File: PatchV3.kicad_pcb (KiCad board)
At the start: 4 copper layers, 100 x 50 mm, 104 parts, among them J1 Conn_01x05, J2 2908-05WB-MG, J3 JST PH SM4 S2B, J4 JST PH SM4 S2B, U1 STM32WB5MMGH6TR_1-, U2 INA317IDGKT, U3 INA317IDGKT, U4 OPA2349EA_250, U5 OPA2349EA_250, U6 ADP5091ACPZ-1-R7, U7 LT3009IDCTRMPBF, U8 LT3009IDCTRMPBF

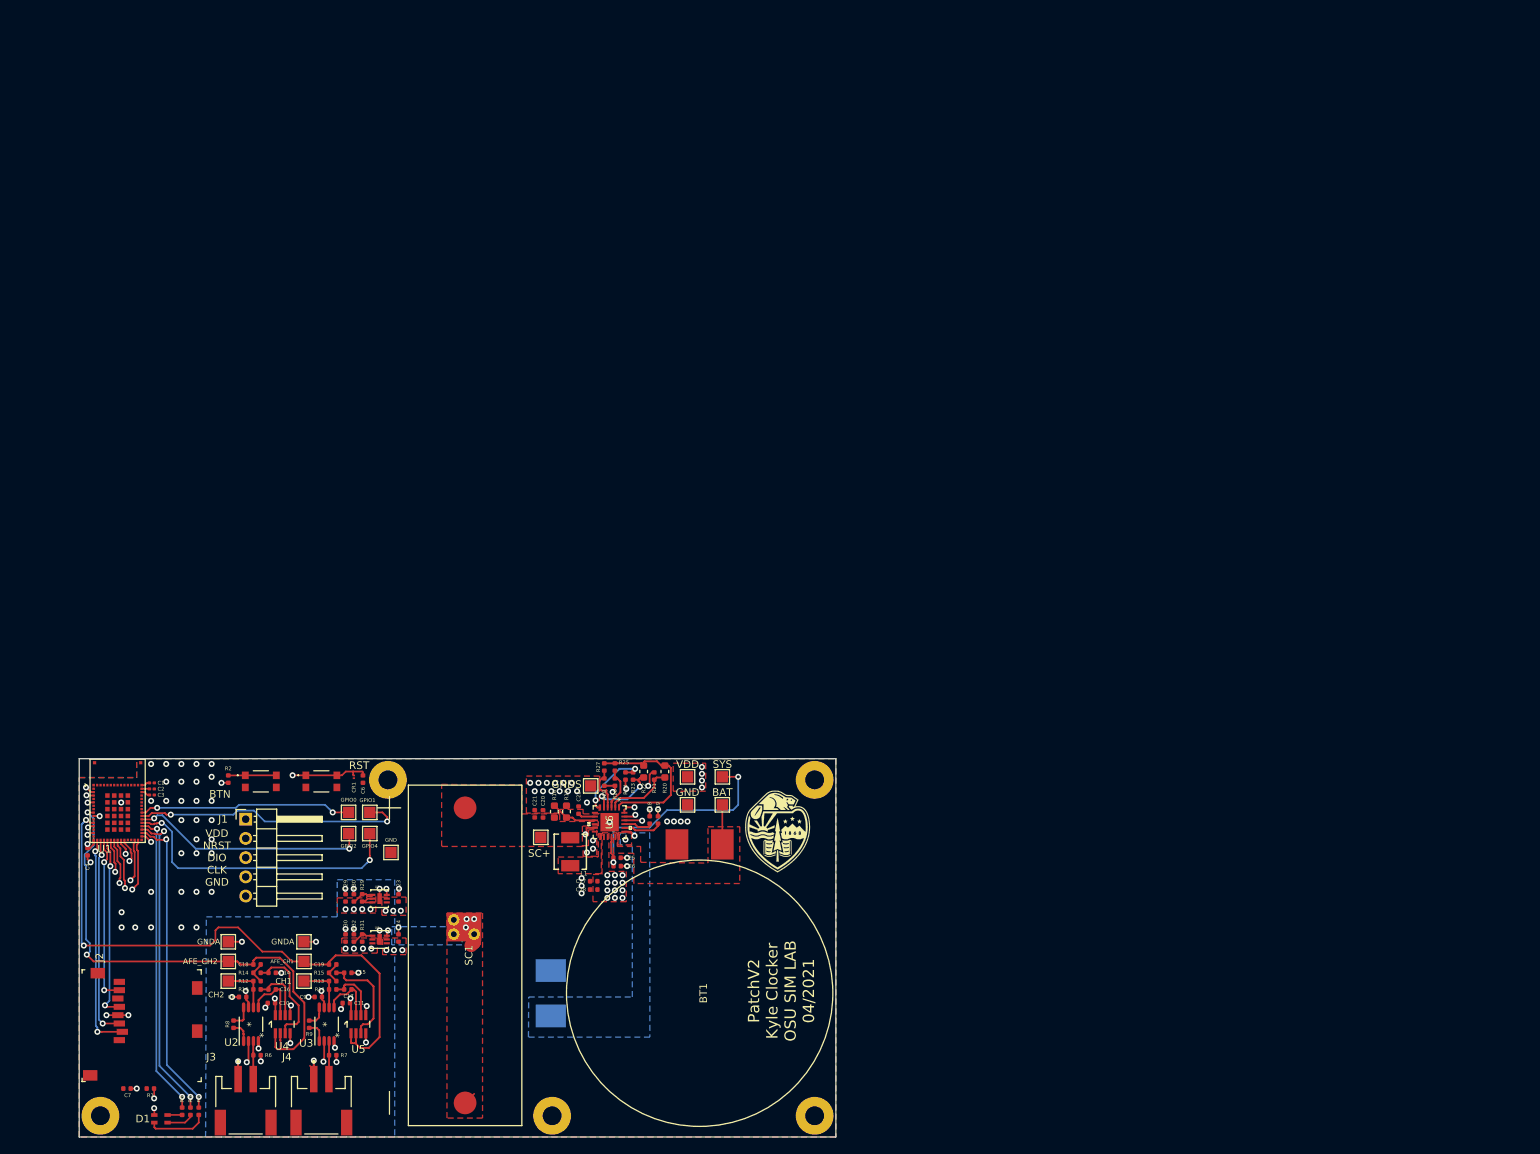
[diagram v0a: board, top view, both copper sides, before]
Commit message: schematic functionally finished working on layout
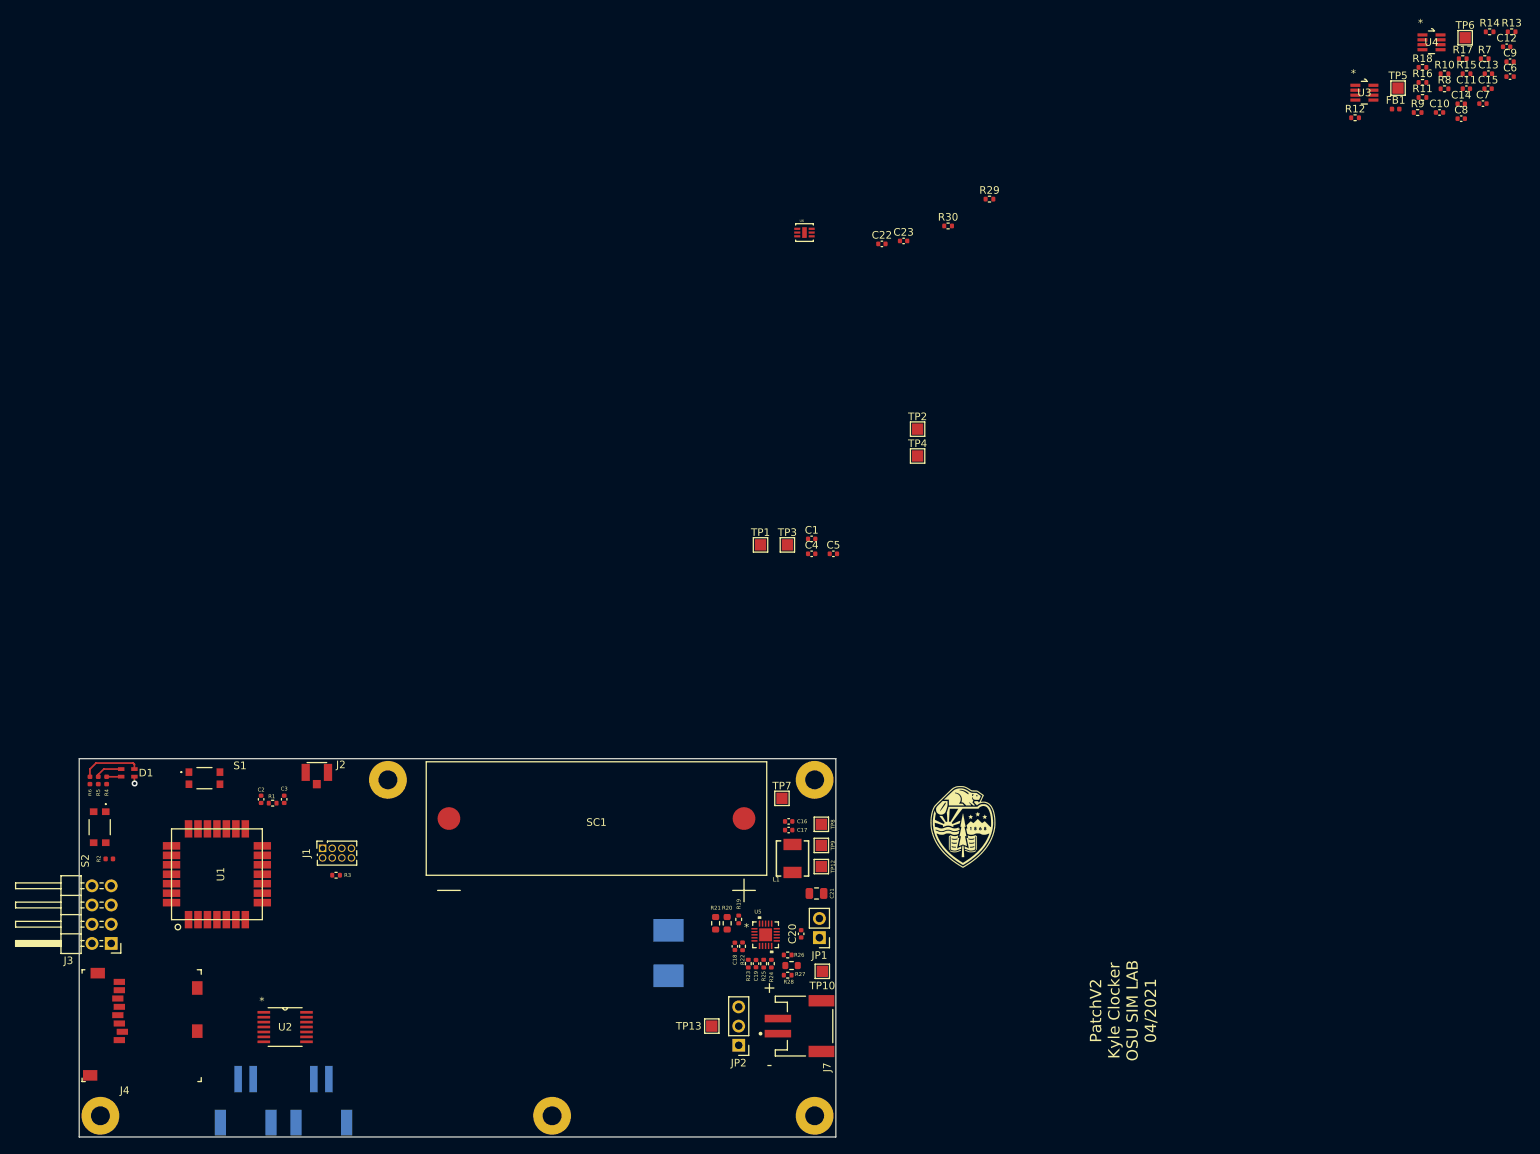
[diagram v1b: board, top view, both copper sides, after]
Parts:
- removed AFE_CH1, AFE_CH2, BAT, CH1, CH2, GND (x2), GNDA (x2), GNDS, GPIO0, GPIO1, GPIO2, GPIO4, SC+, SYS, VDD: TestPoint, TestPoint:TestPoint_Pad_1.5x1.5mm
- removed BT2: 3.7V 500mAh, PatchV2:RJD-ST1
- removed BTN, RST: KMR742NGLFS, PatchV2:KMR742NGLFS
- removed C24, C25, C27, C29, C30: 0.1uF, Capacitor_SMD:C_0402_1005Metric
- removed C26, C28: 10uF, Capacitor_SMD:C_0402_1005Metric
- removed CR1: ESDALC6V1-1U2, PatchV2:ESDALC6V1-1U2
- removed NT1: Net-Tie_3_Tee, PatchV2:gnd_tie
- removed R31: 301k 1%, Resistor_SMD:R_0402_1005Metric
- removed R32: 604k 0.1%, Resistor_SMD:R_0402_1005Metric
- removed the R6 at (73.5, 89.2)
- removed U7, U8: LT3009IDCTRMPBF, PatchV2:DFN-6_DC
- added C12: 0.1uF, Capacitor_SMD:C_0402_1005Metric, F.Cu at (238.7, -44.1)
- added C13: 0.1uF, Capacitor_SMD:C_0402_1005Metric, F.Cu at (236.2, -40.5)
- added C5: 0.1uF, Capacitor_SMD:C_0402_1005Metric, F.Cu at (149.7, 22.9)
- added FB1: 600 Ohm, Inductor_SMD:L_0402_1005Metric, F.Cu at (224.0, -35.9)
- added J2: U.FL-R-SMT(01), PatchV2:HRS_U.FL-R-SMT(01), F.Cu at (81.4, 51.8)
- added J3: Conn_02x04_Odd_Even, Connector_PinHeader_2.54mm:PinHeader_2x04_P2.54mm_Horizontal, F.Cu at (54.2, 74.4)
- added J7: JST PH SM4 S2B, PatchV2:JST-S2B-PH-SM4-TBLFSN-Manufacturer_Recommended, F.Cu at (145.8, 85.3)
- added JP1: Jumper, Connector_PinHeader_2.54mm:PinHeader_1x02_P2.54mm_Vertical, F.Cu at (147.8, 73.7)
- added JP2: Jumper_NC_Dual, Connector_PinHeader_2.54mm:PinHeader_1x03_P2.54mm_Vertical, F.Cu at (137.2, 87.9)
- added R3: 0, Resistor_SMD:R_0402_1005Metric, F.Cu at (83.9, 65.4)
- added S1: KMR742NGLFS, PatchV2:KMR742NGLFS, F.Cu at (66.5, 52.6)
- added S2: KMR742NGLFS, PatchV2:KMR742NGLFS, F.Cu at (52.7, 59.1)
- added TP1: TestPoint, TestPoint:TestPoint_Pad_1.5x1.5mm, F.Cu at (140.0, 21.7)
- added TP10: TestPoint, TestPoint:TestPoint_Pad_1.5x1.5mm, F.Cu at (148.2, 78.1)
- added TP12: TestPoint, TestPoint:TestPoint_Pad_1.5x1.5mm, F.Cu at (148.1, 64.3)
- added TP13: TestPoint, TestPoint:TestPoint_Pad_1.5x1.5mm, F.Cu at (133.6, 85.3)
- added TP2: TestPoint, TestPoint:TestPoint_Pad_1.5x1.5mm, F.Cu at (160.8, 6.45)
- added TP3: TestPoint, TestPoint:TestPoint_Pad_1.5x1.5mm, F.Cu at (143.6, 21.7)
- added TP4: TestPoint, TestPoint:TestPoint_Pad_1.5x1.5mm, F.Cu at (160.8, 9.99)
- added TP5: TestPoint, TestPoint:TestPoint_Pad_1.5x1.5mm, F.Cu at (224.3, -38.6)
- added TP6: TestPoint, TestPoint:TestPoint_Pad_1.5x1.5mm, F.Cu at (233.2, -45.3)
- added TP7: TestPoint, TestPoint:TestPoint_Pad_1.5x1.5mm, F.Cu at (142.9, 55.2)
- added TP8: TestPoint, TestPoint:TestPoint_Pad_1.5x1.5mm, F.Cu at (148.1, 58.7)
- added TP9: TestPoint, TestPoint:TestPoint_Pad_1.5x1.5mm, F.Cu at (148.1, 61.5)
- BT1: moved to B.Cu
- C1: value 3.3pF -> 0.1uF; footprint Capacitor_SMD:C_0201_0603Metric -> Capacitor_SMD:C_0402_1005Metric
- C10, C11: value 0.1uF -> 220p
- C16: value 0.1uF -> 10uF
- C18: value 220p -> 10nF
- C19: value 220p -> 0.1uF
- C2, C3: value 3.3pF -> DNP; footprint Capacitor_SMD:C_0201_0603Metric -> Capacitor_SMD:C_0402_1005Metric
- C21: value 0.1uF -> 47uF; footprint Capacitor_SMD:C_0402_1005Metric -> Capacitor_SMD:C_0805_2012Metric
- C22: value 10nF -> 0.1uF
- J1: value Conn_01x05 -> Conn_02x04_Counter_Clockwise; footprint Connector_PinHeader_2.54mm:PinHeader_1x05_P2.54mm_Horizontal -> Connector_PinSocket_1.27mm:PinSocket_2x04_P1.27mm_Vertical
- J5: renamed from J3; moved to B.Cu
- J6: renamed from J4; moved to B.Cu
- R1: value 10k -> 0
- R10: value 639k 0.1% -> 10k 0.1%
- R11: value 639k 0.1% -> 90.9k 0.1%
- R13, R14: value 90.9k 0.1% -> 632k 0.1%
- R16: value 20M -> 90.9k 0.1%; footprint Resistor_SMD:R_0603_1608Metric -> Resistor_SMD:R_0402_1005Metric
- R17: value 4.7M -> 90.9k 0.1%; footprint Resistor_SMD:R_0603_1608Metric -> Resistor_SMD:R_0402_1005Metric
- R18: value 910k 1% -> 90.9k 0.1%
- R19: value 221k 0.1% -> 0
- R20: value 5.9M -> 1.5M
- R21: value 4.12M -> 8.5M; footprint Resistor_SMD:R_0402_1005Metric -> Resistor_SMD:R_0603_1608Metric
- R22: value 6.19M -> 0; footprint Resistor_SMD:R_0603_1608Metric -> Resistor_SMD:R_0402_1005Metric
- R23: value 73.2k -> 1M 1%
- R24: value 3.83M -> 10M
- R25: value 6.04M -> 10M
- R26: value 4.02M -> 6.04M
- R27: value 6.49M -> 1.05M; footprint Resistor_SMD:R_0402_1005Metric -> Resistor_SMD:R_0603_1608Metric
- R28: value 3.57M -> 2.94M
- R29: value 1.18M 1% -> 1M 1%
- R8: value 5.23k 0.1% -> 1M 0.1%
- R9: value 5.23k 0.1% -> 10k 0.1%
- U1: value STM32WB5MMGH6TR_1- -> LoRa-E5; footprint PatchV2:SiP-LGA86 -> PatchV2:LoRa-E5
- U2: value INA317IDGKT -> INA2321EA_250; footprint PatchV2:INA317IDGKT -> PatchV2:INA2321EA&slash_250
- U3: value INA317IDGKT -> OPA2349EA_250; footprint PatchV2:INA317IDGKT -> PatchV2:OPA2349EA
- U5: value OPA2349EA_250 -> SPV1050TTR; footprint PatchV2:OPA2349EA -> PatchV2:SPV1050TTR
- U6: value ADP5091ACPZ-1-R7 -> LT3009IDCTRMPBF; footprint PatchV2:ADP5091ACPZ-1-R7 -> PatchV2:DFN-6_DC
- moved C7 221.5 mm to (235.5, -36.6), turned to 0 degrees
- moved R14 205.0 mm to (236.4, -46.1), turned to 0 degrees
- moved R8 202.2 mm to (230.4, -38.5), turned to 0 degrees
- moved R7 201.3 mm to (235.8, -42.5), turned to 0 degrees
- moved C9 200.2 mm to (239.1, -42.1), turned to 0 degrees
- moved R13 200.0 mm to (239.3, -46.1), turned to 0 degrees
- moved U4 199.7 mm to (228.7, -44.7), turned to 0 degrees
- moved C8 198.5 mm to (232.7, -34.6), turned to 0 degrees
- moved R10 198.2 mm to (230.4, -40.5), turned to 0 degrees
- moved C14 194.7 mm to (232.7, -36.6)
- moved C10 194.1 mm to (229.8, -35.4), turned to 0 degrees
- moved R15 191.2 mm to (233.4, -40.5), turned to 0 degrees
- moved C11 191.1 mm to (233.3, -38.5), turned to 0 degrees
- moved C15 190.7 mm to (236.2, -38.5)
- moved R9 189.7 mm to (226.9, -35.4), turned to 0 degrees
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- renumbered J2 to J4, R3 to R4, R4 to R5, R5 to R6
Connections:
- BT1 pad 1: /Havester and Power/BAT -> Net-(BT1-Pad1)
- C1 pad 1: /PB10 -> VDD
- C10 pad 1: VDDA -> Net-(C10-Pad1)
- C10 pad 2: GNDA -> VCOM
- C11 pad 1: VDDA -> Net-(C11-Pad1)
- C11 pad 2: GNDA -> VCOM
- C14 pad 1: Net-(C14-Pad1) -> /AFE_CH2
- C14 pad 2: VCOM -> Net-(C14-Pad2)
- C15 pad 1: Net-(C15-Pad1) -> /AFE_CH1
- C15 pad 2: VCOM -> Net-(C15-Pad2)
- C16 pad 1: Net-(C16-Pad1) -> /Havester and Power/SC+
- C16 pad 2: Net-(C16-Pad2) -> GND
- C17 pad 1: Net-(C17-Pad1) -> /Havester and Power/SC+
- C17 pad 2: Net-(C17-Pad2) -> GND
- C18 pad 1: /AFE_CH2 -> Net-(C18-Pad1)
- C18 pad 2: Net-(C18-Pad2) -> GND
- C19 pad 1: /AFE_CH1 -> /LDO_3V3_EN
- C19 pad 2: Net-(C19-Pad2) -> GND
- C2 pad 1: /PB11 -> /RFIO
- C20 pad 1: /Havester and Power/SC+ -> Net-(C20-Pad1)
- C20 pad 2: GNDS -> GND
- C21 pad 1: /Havester and Power/SC+ -> /Havester and Power/STORE
- C21 pad 2: GNDS -> GND
- C22 pad 1: Net-(C22-Pad1) -> VDD
- C22 pad 2: GNDS -> GND
- C23 pad 1: VDD -> VCOM
- C3 pad 1: /PC5 -> /RFIO_ANT
- C4 pad 1: VDD -> /NRST
- C6 pad 1: /NRST -> VDDA
- C7 pad 1: VDD -> VDDA
- C8 pad 2: GNDA -> GND
- C9 pad 2: GNDA -> GND
- J1 pad 1: VDD -> /GPIO2
- J1 pad 2: /NRST -> /GPIO1
- J1 pad 3: /SW_DIO -> /GPIO3
- J1 pad 4: /SW_CLK -> /GPIO0
- J5 pad 1: GNDA -> GND
- J5 pad 2: Net-(J3-Pad2) -> Net-(J5-Pad2)
- J6 pad 1: GNDA -> GND
- J6 pad 2: Net-(J4-Pad2) -> Net-(J6-Pad2)
- L1 pad 2: Net-(L1-Pad2) -> /Havester and Power/SW
- R1 pad 1: /BOOT0 -> /RFIO
- R1 pad 2: GND -> /RFIO_ANT
- R10 pad 1: Net-(C16-Pad2) -> Net-(R10-Pad1)
- R10 pad 2: Net-(R10-Pad2) -> /Contact Mic AFE/REFB
- R11 pad 1: Net-(C17-Pad2) -> Net-(R11-Pad1)
- R12 pad 1: Net-(C18-Pad2) -> Net-(R12-Pad1)
- R12 pad 2: Net-(R10-Pad2) -> Net-(R10-Pad1)
- R13 pad 1: Net-(C19-Pad2) -> Net-(C12-Pad2)
- R13 pad 2: Net-(R11-Pad2) -> Net-(R12-Pad1)
- R14 pad 1: Net-(C14-Pad1) -> Net-(C13-Pad2)
- R14 pad 2: Net-(C18-Pad2) -> Net-(R11-Pad1)
- R15 pad 1: Net-(C15-Pad1) -> Net-(C14-Pad2)
- R15 pad 2: Net-(C19-Pad2) -> Net-(R12-Pad1)
- R16 pad 1: /Havester and Power/SC+ -> Net-(C15-Pad2)
- R16 pad 2: Net-(R16-Pad2) -> Net-(R11-Pad1)
- R17 pad 1: Net-(R16-Pad2) -> Net-(C10-Pad1)
- R17 pad 2: GNDS -> Net-(C14-Pad2)
- R18 pad 1: GNDS -> Net-(C11-Pad1)
- R18 pad 2: Net-(R18-Pad2) -> Net-(C15-Pad2)
- R19 pad 1: GNDS -> /Havester and Power/SC+
- R20 pad 1: /Havester and Power/SETSD -> Net-(R19-Pad2)
- R20 pad 2: /Havester and Power/REF -> Net-(R20-Pad2)
- R21 pad 1: GNDS -> Net-(R20-Pad2)
- R21 pad 2: /Havester and Power/SETSD -> GND
- R22 pad 2: /Havester and Power/REF -> GND
- R23 pad 1: Net-(R23-Pad1) -> /LDO_3V3_EN
- R23 pad 2: Net-(R22-Pad1) -> /Havester and Power/STORE
- R24 pad 1: GNDS -> /Havester and Power/STORE
- R24 pad 2: Net-(R23-Pad1) -> /~BATT_CONN
- R25 pad 1: /Havester and Power/SETBK -> /Havester and Power/STORE
- R25 pad 2: /Havester and Power/REF -> /~BATT_CHG
- R26 pad 1: GNDS -> /Havester and Power/STORE
- R26 pad 2: /Havester and Power/SETBK -> Net-(R26-Pad2)
- R27 pad 1: /Havester and Power/VTERM -> Net-(R26-Pad2)
- R27 pad 2: /Havester and Power/REF -> Net-(R27-Pad2)
- R28 pad 1: GNDS -> Net-(R27-Pad2)
- R28 pad 2: /Havester and Power/VTERM -> GND
- R29 pad 1: VDDA -> VCOM
- R30 pad 2: GNDA -> GND
- R7 pad 2: Net-(J4-Pad2) -> Net-(J5-Pad2)
- R8 pad 1: Net-(R8-Pad1) -> VCOM
- R8 pad 2: Net-(R8-Pad2) -> Net-(J6-Pad2)
- R9 pad 1: Net-(R9-Pad1) -> Net-(R11-Pad2)
- R9 pad 2: Net-(R9-Pad2) -> /Contact Mic AFE/REFA
- SC1 pad 2: GNDS -> GND
- U1 pad 1: Net-(U1-Pad1) -> VDD
- U1 pad 10: /NRST -> /GPIO2
- U1 pad 11: Net-(U1-Pad11) -> /GPIO3
- U1 pad 12: /AFE_CH1 -> /LPUART_TX
- U1 pad 13: /BOOT0 -> /LPUART_RX
- U1 pad 14: Net-(U1-Pad14) -> GND
- U1 pad 15: VDD -> /RFIO
- U1 pad 17: VDD -> /NRST
- U1 pad 18: /SD_CS -> /LED_R
- U1 pad 19: /SD_MOSI -> /LED_G
- U1 pad 2: Net-(U1-Pad2) -> GND
- U1 pad 20: /SD_MISO -> /LED_B
- U1 pad 21: /SD_CLK -> /~BATT_CONN
- U1 pad 22: /PWR_REG_D0 -> GND
- U1 pad 23: /PWR_REG_D1 -> /BTN
- U1 pad 24: /PWR_DIS_SW -> /SD_CLK
- U1 pad 25: /SW_DIO -> /SD_CS
- U1 pad 26: /SW_CLK -> /SD_MISO
- U1 pad 27: Net-(U1-Pad27) -> /SD_MOSI
- U1 pad 3: /BTN -> /SW_DIO
- U1 pad 4: VDD -> /SW_CLK
- U1 pad 5: GND -> /LDO_3V3_EN
- U1 pad 6: VDDA -> /AFE_CH2
- U1 pad 7: Net-(U1-Pad7) -> /AFE_CH1
- U1 pad 8: Net-(U1-Pad8) -> /GPIO0
- U1 pad 9: /AFE_CH2 -> /GPIO1
- U2 pad 1: Net-(R8-Pad2) -> Net-(R11-Pad2)
- U2 pad 3: Net-(J3-Pad2) -> Net-(J6-Pad2)
- U2 pad 4: GNDA -> GND
- U2 pad 5: Net-(C16-Pad1) -> Net-(J5-Pad2)
- U2 pad 6: Net-(R10-Pad2) -> VCOM
- U2 pad 7: VDDA -> Net-(R10-Pad1)
- U2 pad 8: Net-(R8-Pad1) -> Net-(U2-Pad8)
- U3 pad 1: Net-(R9-Pad2) -> /AFE_CH2
- U3 pad 2: VCOM -> /AFE_CH2
- U3 pad 3: Net-(J4-Pad2) -> Net-(C10-Pad1)
- U3 pad 4: GNDA -> GND
- U3 pad 5: Net-(C17-Pad1) -> VCOM
- U3 pad 6: Net-(R11-Pad2) -> Net-(C12-Pad2)
- U3 pad 7: VDDA -> /Contact Mic AFE/REFB
- U3 pad 8: Net-(R9-Pad1) -> VDDA
- U4 pad 1: /AFE_CH2 -> /AFE_CH1
- U4 pad 2: /AFE_CH2 -> /AFE_CH1
- U4 pad 3: Net-(C14-Pad1) -> Net-(C11-Pad1)
- U4 pad 4: GNDA -> GND
- U4 pad 6: Net-(C16-Pad2) -> Net-(C13-Pad2)
- U4 pad 7: Net-(C16-Pad1) -> /Contact Mic AFE/REFA
- U5 pad 1: /AFE_CH1 -> Net-(R19-Pad2)
- U5 pad 2: /AFE_CH1 -> Net-(R20-Pad2)
- U5 pad 3: Net-(C15-Pad1) -> Net-(C18-Pad1)
- U5 pad 4: GNDA -> GND
- U5 pad 5: VCOM -> Net-(R22-Pad1)
- U5 pad 6: Net-(C17-Pad2) -> /LDO_3V3_EN
- U5 pad 7: Net-(C17-Pad1) -> /~BATT_CHG
- U5 pad 8: VDDA -> /~BATT_CONN
- U6 pad 1: /Havester and Power/REF -> Net-(R29-Pad2)
- U6 pad 2: /Havester and Power/SETSD -> VCOM
- U6 pad 3: /Havester and Power/SETBK -> VCOM
- U6 pad 4: /Havester and Power/VTERM -> VDD
- U6 pad 5: Net-(R22-Pad1) -> VDD
- U6 pad 6: Net-(R23-Pad1) -> GND
- U6 pad 7: GNDS -> GND
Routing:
- net /PWR_REG_D0: track 105.3 -> 0.00 mm, vias 2 -> 0
- net /PWR_REG_D1: track 98.5 -> 0.00 mm, vias 2 -> 0
- net /PWR_DIS_SW: track 95.0 -> 0.00 mm, vias 2 -> 0
- net /PWR_PGOOD: track 88.9 -> 0.00 mm, vias 2 -> 0
- net /AFE_CH1: track 78.6 -> 0.00 mm, vias 2 -> 0
- net /PWR_LLD: track 71.7 -> 0.00 mm, vias 2 -> 0
- net /AFE_CH2: track 68.3 -> 0.00 mm, vias 2 -> 0
- net /NRST: track 46.3 -> 0.00 mm, vias 2 -> 0
- net /BOOT0: track 45.4 -> 0.00 mm, vias 2 -> 0
- net /LED_G: track 41.9 -> 0.00 mm, vias 2 -> 0
- net /LED_B: track 41.5 -> 0.00 mm, vias 2 -> 0
- net /LED_R: track 40.5 -> 0.00 mm, vias 2 -> 0
- net /GPIO3: track 39.1 -> 0.00 mm, vias 2 -> 0
- net /GPIO1: track 36.6 -> 0.00 mm, vias 2 -> 0
- net /Havester and Power/SYS: track 31.9 -> 0.00 mm, vias 2 -> 0
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- removed copper zone on F.Cu, net /Havester and Power/BAT
- removed copper zone on F.Cu, net /Havester and Power/SC+
- removed copper zone on B.Cu, net GND
- removed copper zone on F.Cu, net GND
- removed copper zone on B.Cu, net GNDA
- removed copper zone on F.Cu, net GNDS
- removed copper zone on In2.Cu, net GNDS
- removed copper zone on B.Cu, net Net-(BT2-Pad1)
- removed copper zone on F.Cu, net Net-(BT2-Pad1)
- removed copper zone on F.Cu, net Net-(L1-Pad2)
- removed copper zone on F.Cu, net VCOM
- removed copper zone on In2.Cu, net VCOM
- removed copper zone on F.Cu, net VDD
- removed copper zone on In2.Cu, net VDD
- removed copper zone on F.Cu, net VDDA
- removed copper zone on In1.Cu, net VDDA
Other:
- board text added: "+"
- board text added: "-"
- board text removed: "VDD NRST DIO CLK GND"

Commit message: Finished pre-review layout
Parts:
- removed the G*** at (211.1, 66.3)
- removed TP10, TP12, TP13, TP8, TP9: TestPoint, TestPoint:TestPoint_Pad_1.5x1.5mm
- added 1V8: TestPoint, TestPoint:TestPoint_Pad_1.5x1.5mm, F.Cu at (120.9, 98.2)
- added BATT+: TestPoint, TestPoint:TestPoint_Pad_1.5x1.5mm, F.Cu at (117.0, 94.0)
- added C24: 0.1uF, Capacitor_SMD:C_0402_1005Metric, F.Cu at (93.5, 87.4)
- added SC+: TestPoint, TestPoint:TestPoint_Pad_1.5x1.5mm, F.Cu at (137.5, 98.0)
- added STORE: TestPoint, TestPoint:TestPoint_Pad_1.5x1.5mm, F.Cu at (134.5, 98.0)
- added SW: TestPoint, TestPoint:TestPoint_Pad_1.5x1.5mm, F.Cu at (134.5, 94.5)
- R19: value 0 -> 10M; footprint Resistor_SMD:R_0402_1005Metric -> Resistor_SMD:R_0603_1608Metric
- R20: value 1.5M -> 909k
- R21: value 8.5M -> 3.83M
- SC1: footprint PatchV2:SM141K04LV -> PatchV2:SM141K10LV
- moved R14 214.4 mm to (67.7, 86.2), turned to 270 degrees
- moved C13 210.1 mm to (68.7, 86.2), turned to 90 degrees
- moved C7 204.9 mm to (70.7, 85.2)
- moved R13 204.5 mm to (83.4, 86.4), turned to 270 degrees
- moved U4 204.1 mm to (69.1, 82.4), turned to 270 degrees
- moved R8 203.7 mm to (70.9, 88.1), turned to 270 degrees
- moved C11 202.9 mm to (68.2, 79.4), turned to 180 degrees
- moved R7 202.3 mm to (81.3, 88.1), turned to 270 degrees
- moved C12 202.0 mm to (84.5, 86.4), turned to 90 degrees
- moved C6 201.7 mm to (77.0, 79.8), turned to 90 degrees
- moved C15 201.4 mm to (72.6, 79.0)
- moved CH2 199.1 mm to (75.2, 75.9)
- moved R18 197.5 mm to (72.1, 80.5), turned to 90 degrees
- moved C9 197.4 mm to (90.2, 87.4), turned to 270 degrees
- moved R11 195.5 mm to (73.2, 82.5), turned to 270 degrees
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- renumbered TP3 to AFE1, TP4 to AFE2, S2 to BTN, TP5 to CH1, TP6 to CH2, TP7 to GND, TP2 to GND, TP1 to GND, S1 to RST
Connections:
- C14 pad 1: /AFE_CH2 -> /AFE_CH1
- C15 pad 1: /AFE_CH1 -> /AFE_CH2
- J1 pad 6: /AFE_CH1 -> /AFE_CH2
- J1 pad 8: /AFE_CH2 -> /AFE_CH1
- J3 pad 1: /NRST -> /SW_CLK
- J3 pad 4: /LPUART_RX -> /LPUART_TX
- J3 pad 5: /SW_CLK -> /NRST
- J3 pad 6: /LPUART_TX -> /LPUART_RX
- L1 pad 1: /Havester and Power/SC+ -> Net-(L1-Pad1)
- R7 pad 2: Net-(J5-Pad2) -> Net-(J6-Pad2)
- R8 pad 2: Net-(J6-Pad2) -> Net-(J5-Pad2)
- REF** pad 1: GND -> (no net) (x5)
- U2 pad 3: Net-(J6-Pad2) -> Net-(J5-Pad2)
- U2 pad 5: Net-(J5-Pad2) -> Net-(J6-Pad2)
- U3 pad 1: /AFE_CH2 -> /AFE_CH1
- U3 pad 2: /AFE_CH2 -> /AFE_CH1
- U4 pad 1: /AFE_CH1 -> /AFE_CH2
- U4 pad 2: /AFE_CH1 -> /AFE_CH2
- U5 pad 19: GND -> Net-(L1-Pad1)
- U5 pad 20: GND -> /Havester and Power/SC+
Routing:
- net /~BATT_CONN: track 0.00 -> 119.5 mm, vias 0 -> 2
- net /LDO_3V3_EN: track 0.00 -> 103.9 mm, vias 0 -> 4
- net /~BATT_CHG: track 0.00 -> 82.4 mm, vias 0 -> 2
- net /AFE_CH1: track 0.00 -> 41.2 mm, vias 0 -> 1
- net /AFE_CH2: track 0.00 -> 38.5 mm, vias 0 -> 1
- net /NRST: track 0.00 -> 37.0 mm, vias 0 -> 1
- net /LPUART_RX: track 0.00 -> 35.9 mm, vias 0 -> 1
- net /LPUART_TX: track 0.00 -> 35.6 mm, vias 0 -> 2
- net /Havester and Power/STORE: track 0.00 -> 33.4 mm, vias 0 -> 2
- net /SD_CS: track 0.00 -> 27.3 mm, vias 0 -> 2
- net /SD_CLK: track 0.00 -> 25.0 mm, vias 0 -> 2
- net /SD_MOSI: track 0.00 -> 23.9 mm, vias 0 -> 2
- net Net-(R11-Pad1): track 0.00 -> 23.5 mm, vias 0 -> 2
- net Net-(R20-Pad2): track 0.00 -> 21.7 mm
- net /SD_MISO: track 0.00 -> 20.4 mm, vias 0 -> 2
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- added copper zone on In2.Cu, net /Havester and Power/SC+
- added copper zone on B.Cu, net GND
- added copper zone on F.Cu, net GND
- added copper zone on In1.Cu, net GND
- added copper zone on B.Cu, net Net-(BT1-Pad1)
- added copper zone on B.Cu, net VCOM
- added copper zone on In2.Cu, net VDD
- added copper zone on In2.Cu, net VDDA
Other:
- net class Default: trace_width 0.2286 -> 0.1778; via_dia 0.8 -> 0.7; via_drill 0.4 -> 0.35
- net class RF added: clearance 0.1524, trace_width 0.2921, via_dia 0.7, via_drill 0.35
- board text added: "GND NRST DIO CLK"
- board text added: "GND RX TX VDD"
- board text added: "PatchV3.0 08/2021 Kyle Clocker OSU SIM LAB"
- board text removed: "PatchV2 Kyle Clocker OSU SIM LAB 04/2021"

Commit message: fixed a position of a pin header
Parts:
- moved JP2 7.92 mm to (117.3, 97.9), turned to 180 degrees
- moved BATT+ 4.86 mm to (112.4, 92.5), turned to 90 degrees
- moved 1V8 0.65 mm to (121.5, 98.3)
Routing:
- net /Havester and Power/BATT_CHG: track 8.43 -> 15.0 mm
- net /Havester and Power/BATT: track 13.4 -> 12.7 mm
- net Net-(TP10-Pad1): track 8.79 -> 8.18 mm
